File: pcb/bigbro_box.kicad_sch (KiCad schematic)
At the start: 52 parts, among them J1 Current Sense, J2 Display, J3 Mains, J4 Debug, J5 RFID, J6 Relay, J7 Ext, K1 G5LE-1, Q1 MMBT3904, Q2 MMBT3904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

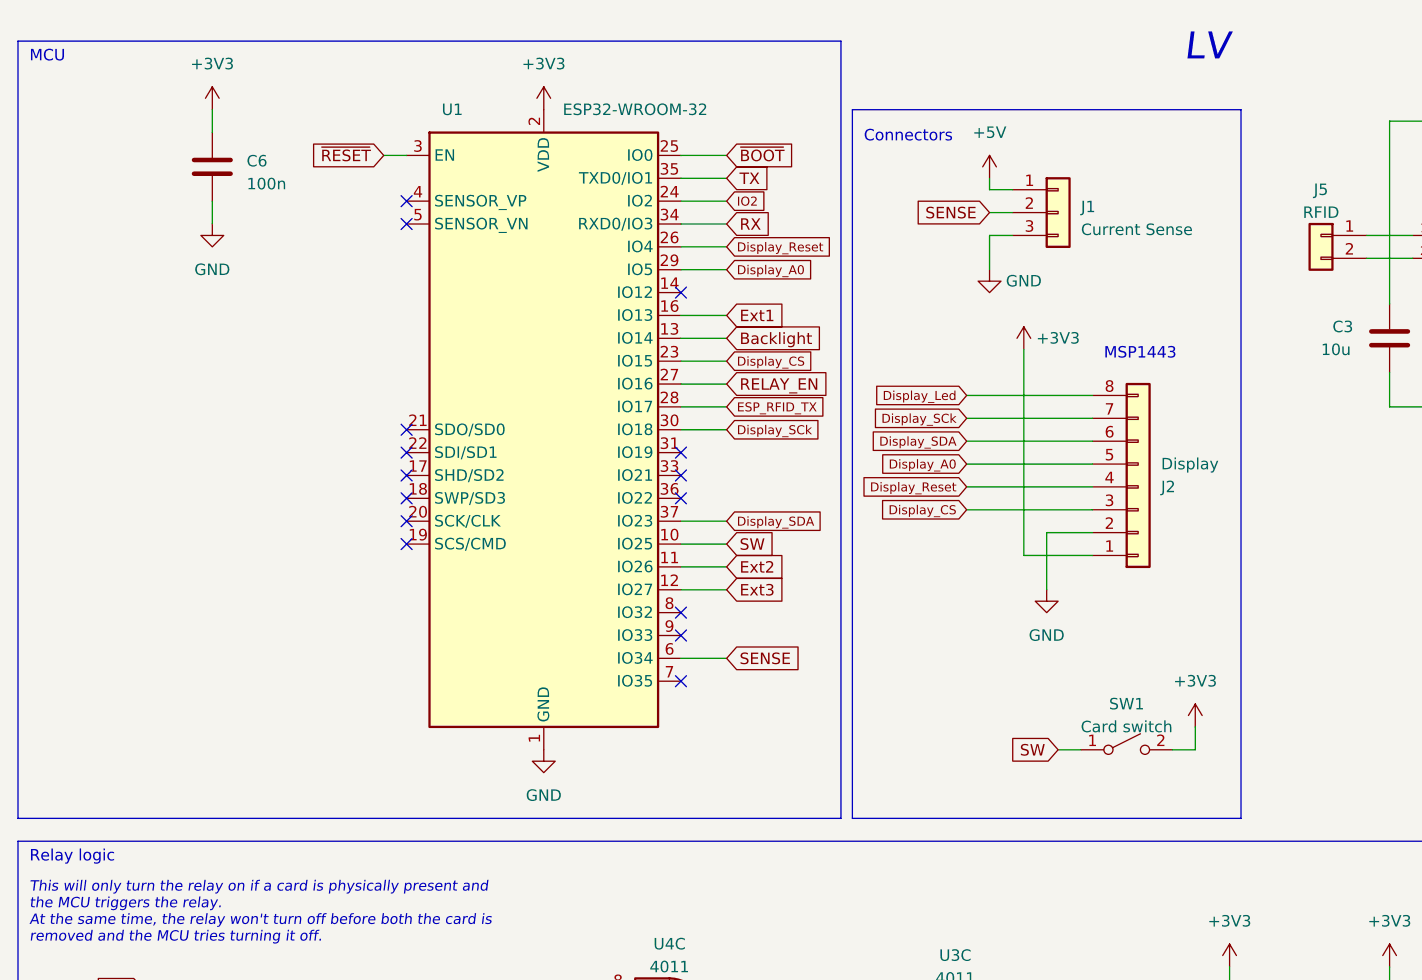
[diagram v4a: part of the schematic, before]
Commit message: Add resistor divider for current sense input.
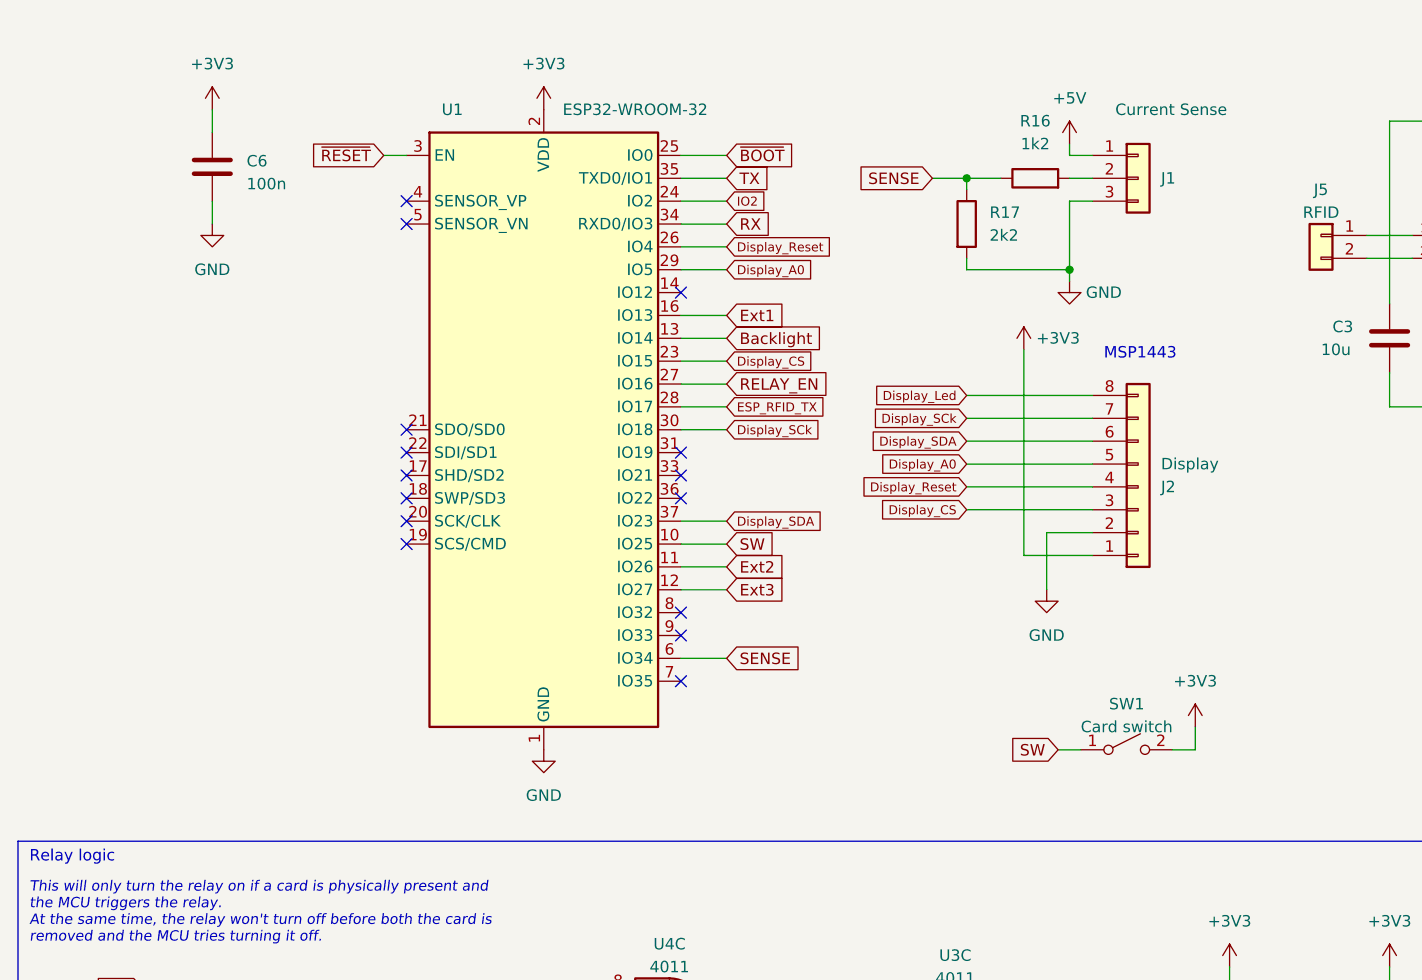
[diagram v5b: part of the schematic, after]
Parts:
- added R16: 1k2, PCM_Resistor_SMD_AKL:R_0603_1608Metric, symbol Device:R
- added R17: 2k2, PCM_Resistor_SMD_AKL:R_0603_1608Metric, symbol Device:R
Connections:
- net GND: now also R17.2
- net SENSE: now also R16.1, R17.1; no longer J1.2 (Pin_2)
- new net: J1.2 (Pin_2), R16.2
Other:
- note removed: "Connectors"
- note removed: "LV"
- note removed: "MCU"
- moved on the sheet: J1

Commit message: Use zener.
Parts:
- removed R17: 2k2, PCM_Resistor_SMD_AKL:R_0603_1608Metric, symbol Device:R
- added D4: 3V0, Diode_SMD:D_MiniMELF, symbol PCM_Diode_Zener_AKL:D_Zener_Generic
- R16: value 1k2 -> 1k
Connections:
- net GND: now also D4.2 (A)
- net SENSE: now also D4.1 (K)
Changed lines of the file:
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@@
-	)
-	(symbol
-		(lib_id "Device:R")
-		(at 120.65 36.83 0)
-		(unit 1)
-		(exclude_from_sim no)
-		(in_bom yes)
-		(on_board yes)
-		(dnp no)
-		(fields_autoplaced yes)
-		(property "Reference" "R17"
-			(at 123.19 35.5599 0)
-			(effects
-				(font
-					(size 1.27 1.27)
-				)
-				(justify left)
-			)
-		)
-		(property "Value" "2k2"
-			(at 123.19 38.0999 0)
-			(effects
-				(font
-					(size 1.27 1.27)
-				)
-				(justify left)
-			)
-		)
-		(property "Footprint" "PCM_Resistor_SMD_AKL:R_0603_1608Metric"
-			(at 118.872 36.83 90)
-			(effects
-				(font
-					(size 1.27 1.27)
-				)
-				(hide yes)
-			)
-		)
-		(property "Datasheet" "~"
-			(at 120.65 36.83 0)
-			(effects
-				(font
-					(size 1.27 1.27)
-				)
-				(hide yes)
-			)
-		)
-		(property "Description" "Resistor"
-			(at 120.65 36.83 0)
-			(effects
-				(font
-					(size 1.27 1.27)
-				)
-				(hide yes)
-			)
-		)
-		(pin "1"
-		)
-		(pin "2"
-		)
-		(instances
-			(project ""
-				(path "/212a0d71-cc7b-49f8-b4ca-a935e5355dca"
-					(reference "R17")
-					(unit 1)
-				)
-			)
-		)
 	)
 	(symbol
@@
 	)
 	(symbol
+		(lib_id "PCM_Diode_Zener_AKL:D_Zener_Generic")
+		(at 120.65 36.83 90)
+		(unit 1)
+		(exclude_from_sim no)
+		(in_bom yes)
+		(on_board yes)
+		(dnp no)
+		(fields_autoplaced yes)
+		(property "Reference" "D4"
+			(at 123.19 35.5599 90)
+			(effects
+				(font
+					(size 1.27 1.27)
+				)
+				(justify right)
+			)
+		)
+		(property "Value" "3V0"
+			(at 123.19 38.0999 90)
+			(effects
+				(font
+					(size 1.27 1.27)
+				)
+				(justify right)
+			)
+		)
+		(property "Footprint" "Diode_SMD:D_MiniMELF"
+			(at 120.65 36.83 0)
+			(effects
+				(font
+					(size 1.27 1.27)
+				)
+				(hide yes)
+			)
+		)
+		(property "Datasheet" "~"
+			(at 120.65 36.83 0)
+			(effects
+				(font
+					(size 1.27 1.27)
+				)
+				(hide yes)
+			)
+		)
+		(property "Description" "Zener diode, generic symbol, Alternate KiCAD Library"
+			(at 120.65 36.83 0)
+			(effects
+				(font
+					(size 1.27 1.27)
+				)
+				(hide yes)
+			)
+		)
+		(pin "2"
+		)
+		(pin "1"
+		)
+		(instances
+			(project ""
+				(path "/212a0d71-cc7b-49f8-b4ca-a935e5355dca"
+					(reference "D4")
+					(unit 1)
+				)
+			)
+		)
+	)
+	(symbol
 		(lib_id "4xxx:4011")
 		(at 119.38 173.99 0)
@@
 			)
 		)
-		(property "Value" "1k2"
+		(property "Value" "1k"
 			(at 128.27 27.94 90)
 			(effects

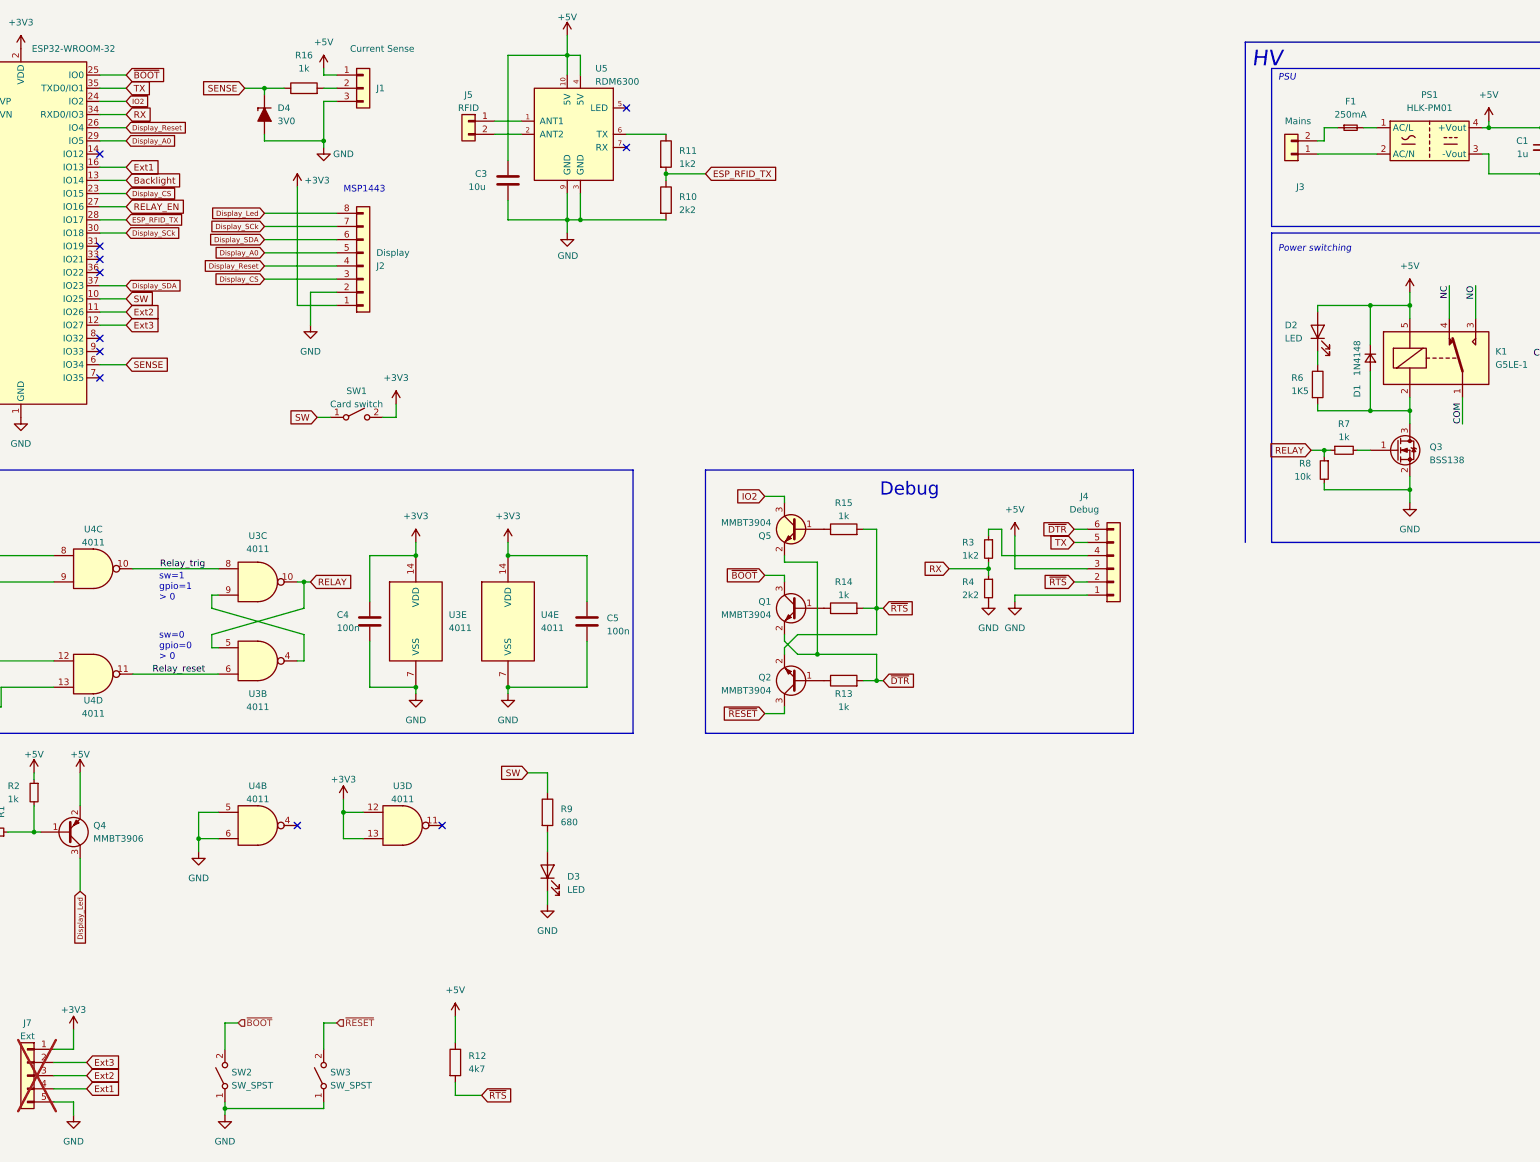
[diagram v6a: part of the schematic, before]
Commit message: Simplify debug circuitry.
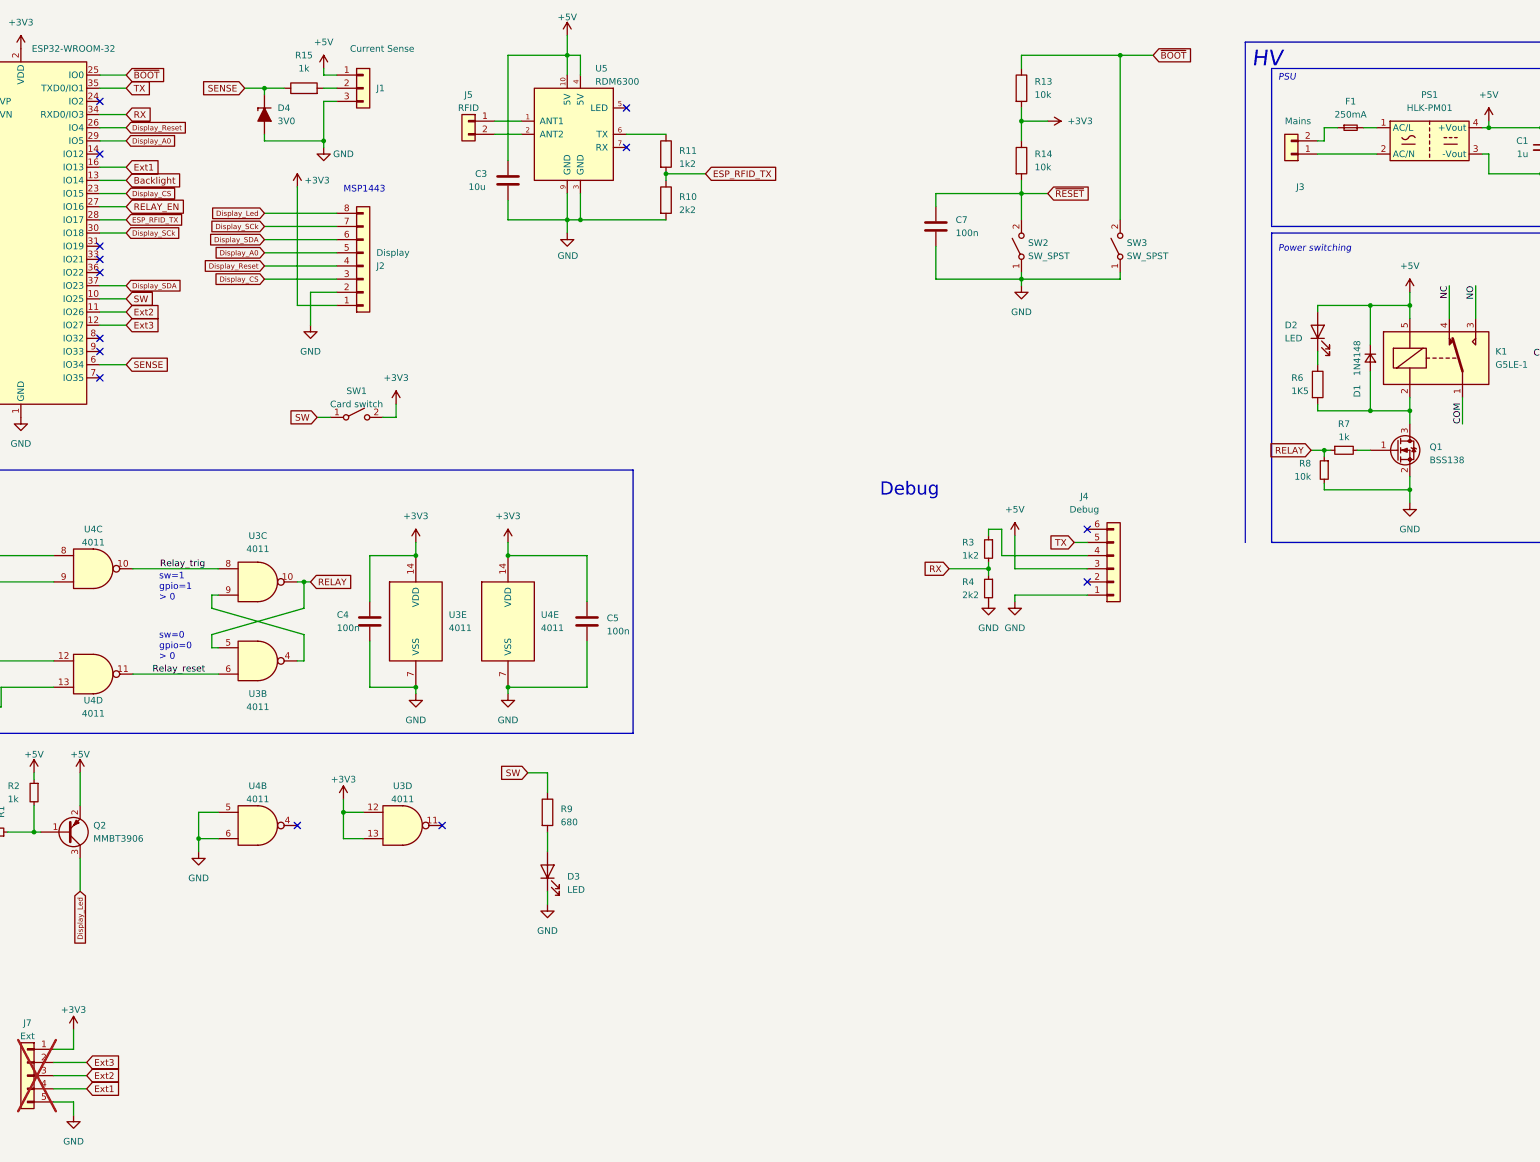
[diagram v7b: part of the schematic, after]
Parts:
- removed Q1, Q2: MMBT3904, PCM_Package_TO_SOT_SMD_AKL:SOT-23, symbol Transistor_BJT:MMBT3904
- removed Q5: MMBT3904, PCM_Package_TO_SOT_SMD_AKL:SOT-23, symbol PCM_Transistor_BJT_AKL:MMBT3904
- removed R12: 4k7, PCM_Resistor_SMD_AKL:R_0603_1608Metric, symbol Device:R
- removed R15: 1k, PCM_Resistor_SMD_AKL:R_0603_1608Metric, symbol Device:R
- added C7: 100n, Capacitor_SMD_AKL:C_0603_1608Metric, symbol Device:C
- C1, C2, C3, C4, C5, C6: footprint PCM_Capacitor_SMD_AKL:C_0603_1608Metric -> Capacitor_SMD_AKL:C_0603_1608Metric
- D2, D3: footprint PCM_LED_SMD_AKL:LED_0603_1608Metric -> LED_SMD:LED_0603_1608Metric
- Q1: renamed from Q3; footprint PCM_Package_TO_SOT_SMD_AKL:SOT-23 -> Package_TO_SOT_SMD:SOT-23
- Q2: renamed from Q4; footprint PCM_Package_TO_SOT_SMD_AKL:SOT-23 -> Package_TO_SOT_SMD:SOT-23
- R1, R10, R11, R2, R3, R4, R5, R6, R7, R8, R9: footprint PCM_Resistor_SMD_AKL:R_0603_1608Metric -> Resistor_SMD_AKL:R_0603_1608Metric
- R13, R14: value 1k -> 10k; footprint PCM_Resistor_SMD_AKL:R_0603_1608Metric -> Resistor_SMD_AKL:R_0603_1608Metric; LCSC C14676 -> (none)
- R15: renamed from R16; footprint PCM_Resistor_SMD_AKL:R_0603_1608Metric -> Resistor_SMD_AKL:R_0603_1608Metric
- U2: footprint PCM_Package_TO_SOT_SMD_AKL:SOT-223-3_TabPin2 -> Package_TO_SOT_SMD:SOT-223-3_TabPin2
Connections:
- net +3V3: now also R13.2, R14.1
- net GND: now also C7.2
- net ~{BOOT}: now also R13.1, SW3.2 (B); no longer SW2.2 (B)
- net ~{RESET}: now also R14.2, SW2.2 (B), C7.1; no longer SW3.2 (B)
- net IO2: no longer names the net of U1.24 (IO2)
- net ~{DTR}: no longer names the net of J4.6 (Pin_6)
- net ~{DTR}: no longer R13.2
- net ~{RTS}: no longer names the net of J4.2 (Pin_2)
- net ~{RTS}: no longer R14.2
- no-connect marks 19 -> 22

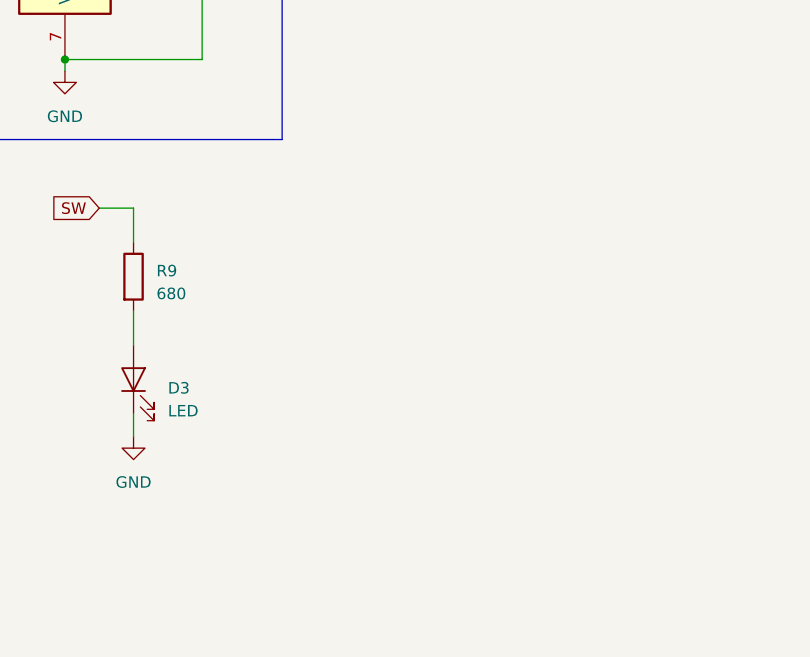
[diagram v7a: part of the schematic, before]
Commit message: Add power LEDs.
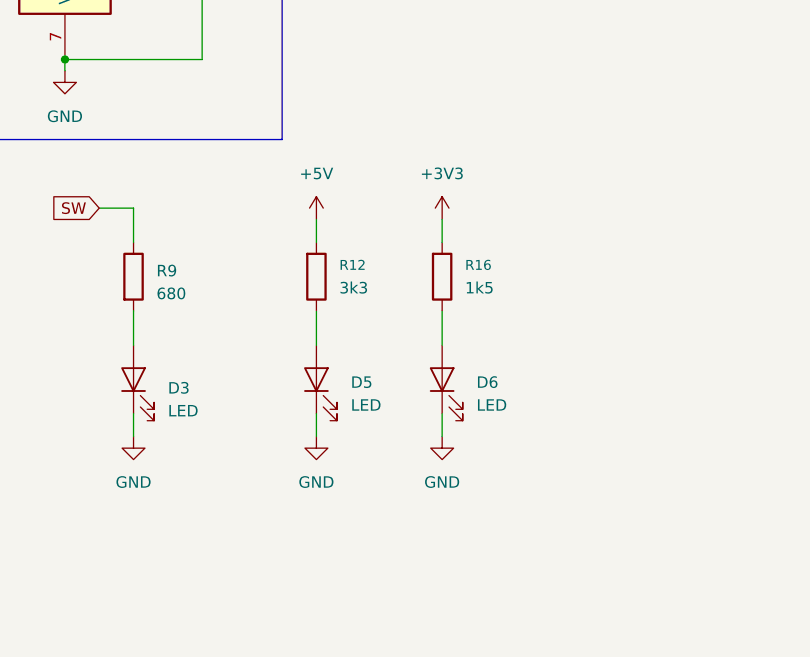
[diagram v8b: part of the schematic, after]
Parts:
- added D5, D6: LED, LED_SMD:LED_0603_1608Metric, symbol Device:LED
- added R12: 3k3, Resistor_SMD_AKL:R_0603_1608Metric, symbol kicadunlocked:R
- added R16: 1k5, Resistor_SMD_AKL:R_0603_1608Metric, symbol kicadunlocked:R
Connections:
- net +3V3: now also R16.1
- net +5V: now also R12.1
- net GND: now also D5.1 (K), D6.1 (K)
- new net: D5.2 (A), R12.2
- new net: D6.2 (A), R16.2
